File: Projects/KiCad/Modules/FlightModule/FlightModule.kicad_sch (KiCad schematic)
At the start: 59 parts, among them J1 Conn_01x08, J2 Conn_01x02_Pin, J3 Conn_01x02_Pin, J4 Conn_01x02_Pin, J5 Conn_01x02_Pin, J6 Conn_01x02_Pin, Q1 DTC143E, SW1 SW_DIP_x02, U1 MCP2562-E-P, U2 NUCLEO-F303K8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

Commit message: チップ積層セラミックコンデンサをSMD1608に変更
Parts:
- C1, C2, C4: footprint Capacitor_SMD:C_0805_2012Metric_Pad1.18x1.45mm_HandSolder -> Capacitor_SMD:C_0603_1608Metric_Pad1.08x0.95mm_HandSolder
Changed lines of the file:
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@@
       (effects (font (size 1.27 1.27)) (justify left))
     )
-    (property "Footprint" "Capacitor_SMD:C_0805_2012Metric_Pad1.18x1.45mm_HandSolder" (at 88.5952 35.56 0)
+    (property "Footprint" "Capacitor_SMD:C_0603_1608Metric_Pad1.08x0.95mm_HandSolder" (at 88.5952 35.56 0)
       (effects (font (size 1.27 1.27)) hide)
     )
@@
       (effects (font (size 1.27 1.27)) (justify left))
     )
-    (property "Footprint" "Capacitor_SMD:C_0805_2012Metric_Pad1.18x1.45mm_HandSolder" (at 79.7052 35.56 0)
+    (property "Footprint" "Capacitor_SMD:C_0603_1608Metric_Pad1.08x0.95mm_HandSolder" (at 79.7052 35.56 0)
       (effects (font (size 1.27 1.27)) hide)
     )
@@
       (effects (font (size 1.27 1.27)) (justify left))
     )
-    (property "Footprint" "Capacitor_SMD:C_0805_2012Metric_Pad1.18x1.45mm_HandSolder" (at 121.6152 109.22 0)
-      (effects (font (size 1.27 1.27)) hide)
-    )
+    (property "Footprint" "Capacitor_SMD:C_0603_1608Metric_Pad1.08x0.95mm_HandSolder" (at 121.6152 109.22 0)
+      (effects (font (size 1.27 1.27)) hide)
+    )

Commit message: 抵抗の在庫に合わせてサイズを変更
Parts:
- R23, R24, R5, R6: footprint Resistor_SMD:R_0603_1608Metric_Pad0.98x0.95mm_HandSolder -> Resistor_SMD:R_0805_2012Metric_Pad1.20x1.40mm_HandSolder
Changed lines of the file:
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@@
       (effects (font (size 1.27 1.27)) (justify left))
     )
-    (property "Footprint" "Resistor_SMD:R_0603_1608Metric_Pad0.98x0.95mm_HandSolder" (at 106.172 92.71 90)
+    (property "Footprint" "Resistor_SMD:R_0805_2012Metric_Pad1.20x1.40mm_HandSolder" (at 106.172 92.71 90)
       (effects (font (size 1.27 1.27)) hide)
     )
@@
       (effects (font (size 1.27 1.27)) (justify left))
     )
-    (property "Footprint" "Resistor_SMD:R_0603_1608Metric_Pad0.98x0.95mm_HandSolder" (at 182.372 49.53 90)
+    (property "Footprint" "Resistor_SMD:R_0805_2012Metric_Pad1.20x1.40mm_HandSolder" (at 182.372 49.53 90)
       (effects (font (size 1.27 1.27)) hide)
     )
@@
       (effects (font (size 1.27 1.27)))
     )
-    (property "Footprint" "Resistor_SMD:R_0603_1608Metric_Pad0.98x0.95mm_HandSolder" (at 114.3 97.282 90)
+    (property "Footprint" "Resistor_SMD:R_0805_2012Metric_Pad1.20x1.40mm_HandSolder" (at 114.3 97.282 90)
       (effects (font (size 1.27 1.27)) hide)
     )
@@
       (effects (font (size 1.27 1.27)) (justify left))
     )
-    (property "Footprint" "Resistor_SMD:R_0603_1608Metric_Pad0.98x0.95mm_HandSolder" (at 172.212 49.53 90)
-      (effects (font (size 1.27 1.27)) hide)
-    )
+    (property "Footprint" "Resistor_SMD:R_0805_2012Metric_Pad1.20x1.40mm_HandSolder" (at 172.212 49.53 90)
+      (effects (font (size 1.27 1.27)) hide)
+    )

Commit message: コネクタのピン配置を変更
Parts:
- J1: footprint Connector_Hirose:Hirose_DF11-8DP-2DSA_2x04_P2.00mm_Vertical -> Hirose_Connector:Hirose_DF11B-8DP-2DS
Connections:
- net CAN_L: now also J1.5 (Pin_5), J1.6 (Pin_6); no longer J1.3 (Pin_3), J1.4 (Pin_4)
- net GND: now also J1.3 (Pin_3), J1.4 (Pin_4); no longer J1.5 (Pin_5), J1.6 (Pin_6)
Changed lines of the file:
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@@
-    (effects (font (size 1.27 1.27)) (justify right bottom))
-  )
-  (label "CAN_L" (at 36.83 36.83 180) (fields_autoplaced)
-    (effects (font (size 1.27 1.27)) (justify right bottom))
-  )
-  (label "GND" (at 36.83 31.75 180) (fields_autoplaced)
     (effects (font (size 1.27 1.27)) (justify right bottom))
   )
@@
     (effects (font (size 1.27 1.27)) (justify right bottom))
   )
+  (label "GND" (at 36.83 36.83 180) (fields_autoplaced)
+    (effects (font (size 1.27 1.27)) (justify right bottom))
+  )
   (label "GND" (at 41.91 57.15 0) (fields_autoplaced)
     (effects (font (size 1.27 1.27)) (justify left bottom))
   )
+  (label "CAN_H" (at 36.83 26.67 180) (fields_autoplaced)
+    (effects (font (size 1.27 1.27)) (justify right bottom))
+  )
   (label "+12V" (at 41.91 54.61 0) (fields_autoplaced)
     (effects (font (size 1.27 1.27)) (justify left bottom))
   )
-  (label "CAN_H" (at 36.83 26.67 180) (fields_autoplaced)
+  (label "CAN_L" (at 36.83 31.75 180) (fields_autoplaced)
     (effects (font (size 1.27 1.27)) (justify right bottom))
   )
@@
       (effects (font (size 1.27 1.27)))
     )
-    (property "Footprint" "Connector_Hirose:Hirose_DF11-8DP-2DSA_2x04_P2.00mm_Vertical" (at 20.32 35.56 0)
-      (effects (font (size 1.27 1.27)) hide)
-    )
+    (property "Footprint" "Hirose_Connector:Hirose_DF11B-8DP-2DS" (at 20.32 35.56 0)
+      (effects (font (size 1.27 1.27)) hide)
+    )

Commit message: バッファコンデンサを表面実装に変更
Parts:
- C3: value 100μF -> 47μF; footprint Capacitor_SMD:CP_Elec_6.3x7.7 -> Capacitor_SMD:CP_Elec_6.3x5.9
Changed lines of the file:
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@@
       (effects (font (size 1.27 1.27)) (justify left))
     )
-    (property "Value" "100μF" (at 186.69 124.206 0)
+    (property "Value" "47μF" (at 186.69 124.206 0)
       (effects (font (size 1.27 1.27)) (justify left))
     )
-    (property "Footprint" "Capacitor_SMD:CP_Elec_6.3x7.7" (at 183.8452 127 0)
+    (property "Footprint" "Capacitor_SMD:CP_Elec_6.3x5.9" (at 183.8452 127 0)
       (effects (font (size 1.27 1.27)) hide)
     )

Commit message: チェックよし（多分）
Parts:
- removed Q1: DTC143E, Package_TO_SOT_THT:TO-92_Inline, symbol Transistor_BJT:DTC143E
- added Q1: Q_NPN_BEC, Package_TO_SOT_SMD:SC-59_Handsoldering, symbol Device:Q_NPN_BEC
- added R26, R27: 4.7kΩ, Resistor_SMD:R_0603_1608Metric_Pad0.98x0.95mm_HandSolder, symbol Device:R
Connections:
- net CONTROL_CAMERA: now also R26.1
- net at J6.1 (Pin_1): now also Q1.2 (E), R27.1
- net at J6.2 (Pin_2): now also Q1.3 (C)
- new net: Q1.1 (B), R26.2, R27.2
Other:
- moved on the sheet: D10, J6, R13

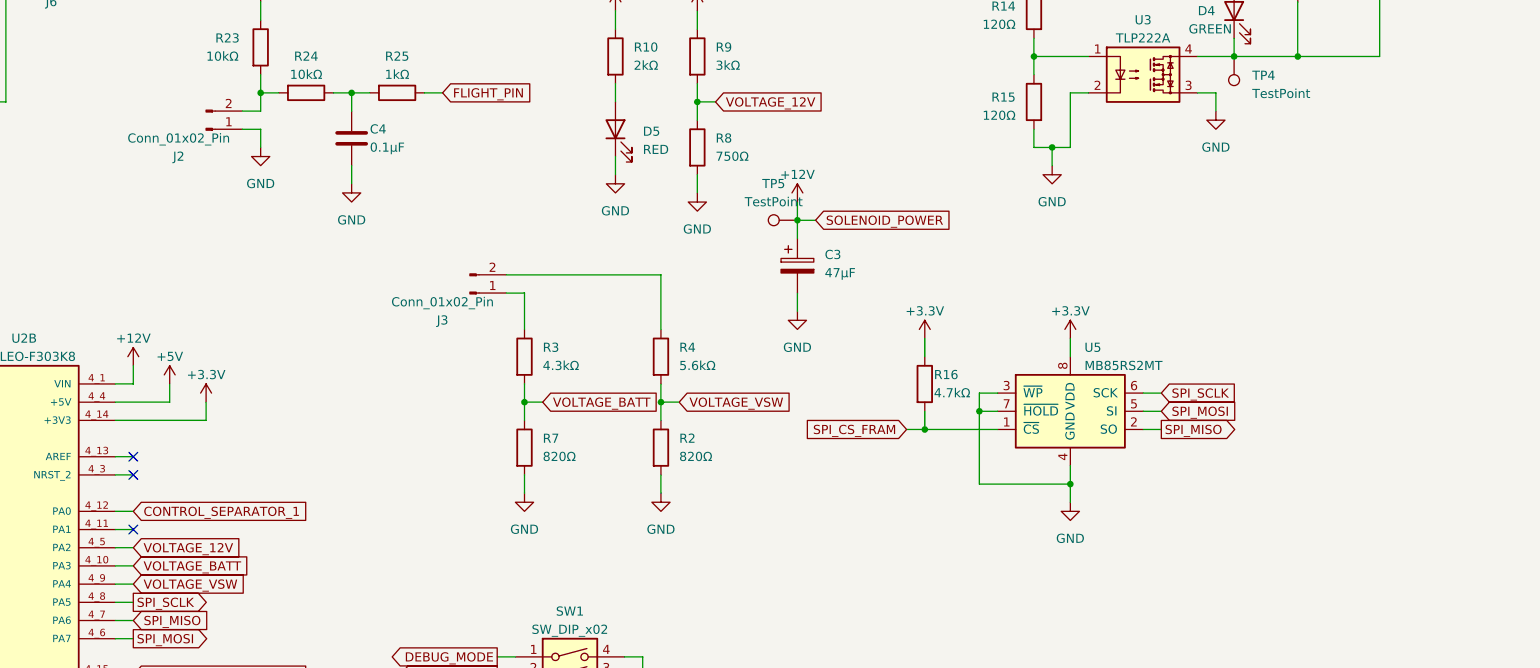
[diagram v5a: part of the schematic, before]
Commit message: フライトモジュールにブザーを追加
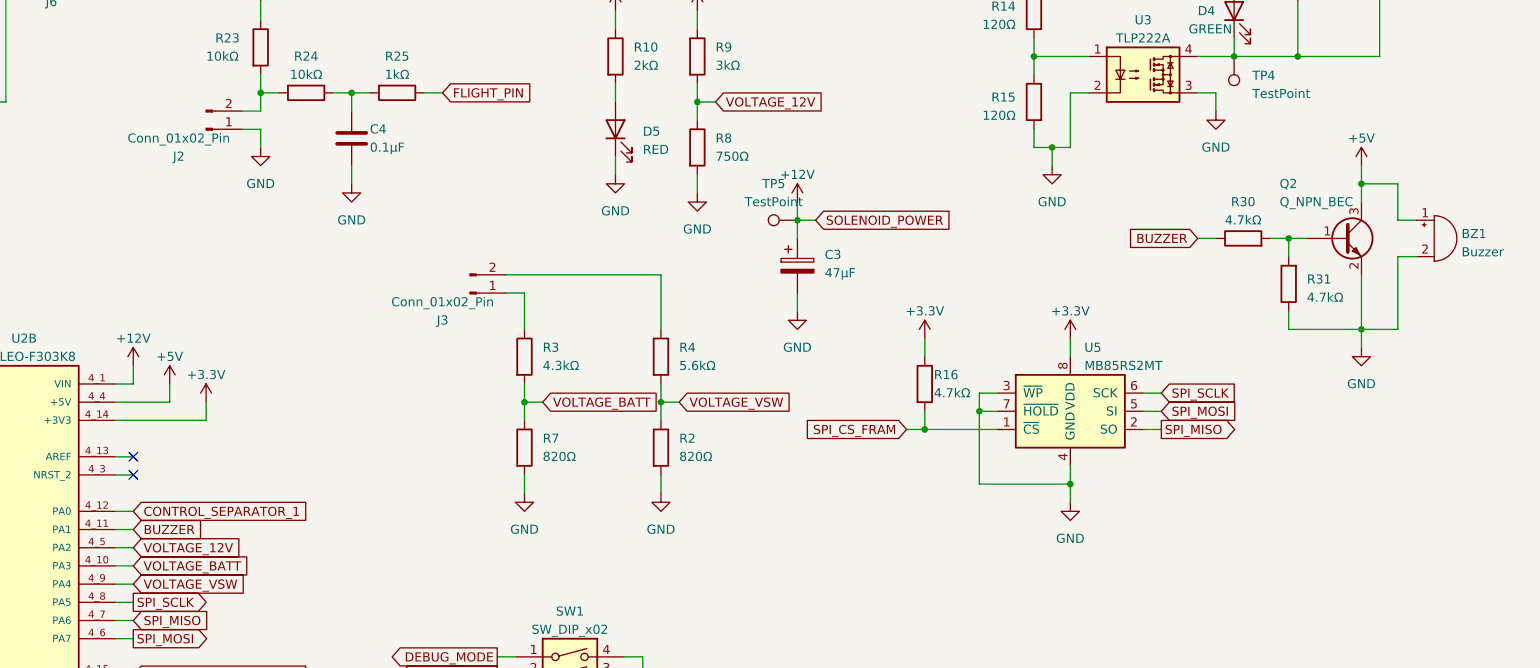
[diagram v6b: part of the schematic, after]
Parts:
- added BZ1: Buzzer, Buzzer_Beeper:Buzzer_12x9.5RM7.6, symbol Device:Buzzer
- added Q2: Q_NPN_BEC, Package_TO_SOT_SMD:SC-59_Handsoldering, symbol Device:Q_NPN_BEC
- added R30, R31: 4.7kΩ, Resistor_SMD:R_0603_1608Metric_Pad0.98x0.95mm_HandSolder, symbol Device:R
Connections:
- net +5V: now also BZ1.1 (-), Q2.3 (C)
- net GND: now also BZ1.2 (+), Q2.2 (E), R31.1
- net BUZZER: now reaches U2.4_11 (PA1)
- net BUZZER: now also R30.1
- new net: Q2.1 (B), R30.2, R31.2
- no-connect marks 4 -> 3

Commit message: フライトモジュールのGNDにテストポイントを追加
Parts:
- added TP6: TestPoint, Connector_Pin:Pin_D1.0mm_L10.0mm, symbol Connector:TestPoint
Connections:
- net GND: now also TP6.1
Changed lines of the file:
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@@
   (junction (at 200.66 146.05) (diameter 0) (color 0 0 0 0)
+  )
+  (junction (at 53.34 57.15) (diameter 0) (color 0 0 0 0)
   )
   (junction (at 261.62 132.08) (diameter 0) (color 0 0 0 0)
@@
         )
       )
+    )
+  )
+  (symbol (lib_id "Connector:TestPoint") (at 53.34 57.15 270) (unit 1)
+    (in_bom yes) (on_board yes) (dnp no) (fields_autoplaced)
+    (property "Reference" "TP6" (at 58.42 56.515 90)
+      (effects (font (size 1.27 1.27)) (justify left))
+    )
+    (property "Value" "TestPoint" (at 58.42 59.055 90)
+      (effects (font (size 1.27 1.27)) (justify left))
+    )
+    (property "Footprint" "Connector_Pin:Pin_D1.0mm_L10.0mm" (at 53.34 62.23 0)
+      (effects (font (size 1.27 1.27)) hide)
+    )
+    (property "Datasheet" "~" (at 53.34 62.23 0)
+      (effects (font (size 1.27 1.27)) hide)
+    )
+    (pin "1")
+    (instances
+      (project "FlightModule"
+        (path "/ea1ed597-7cd3-4340-902e-bdce8f2d7a62"
+          (reference "TP6") (unit 1)
+        )
+      )

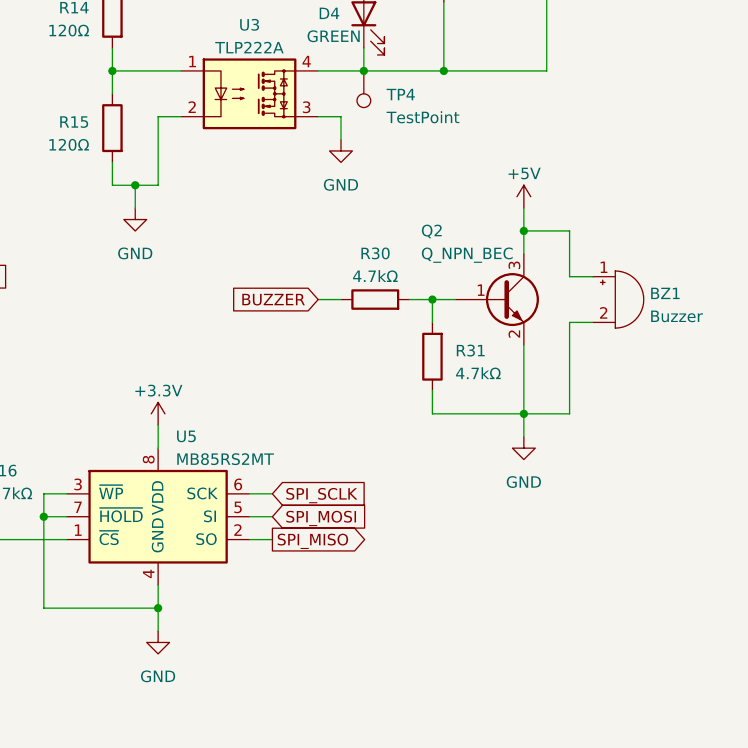
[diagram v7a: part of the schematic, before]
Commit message: ブザーの回路を修正
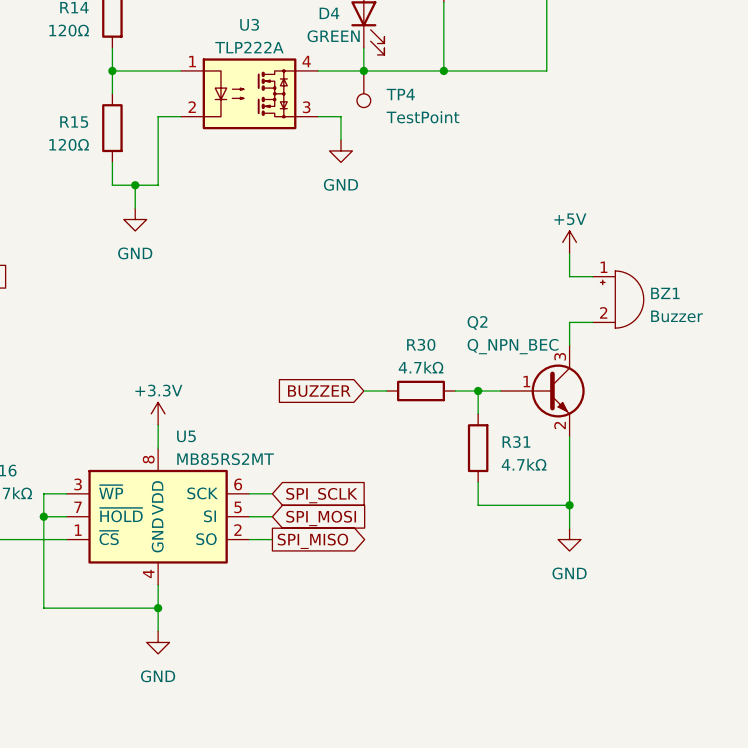
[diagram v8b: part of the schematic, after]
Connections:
- net +5V: no longer Q2.3 (C)
- net GND: no longer BZ1.2 (+)
- new net: BZ1.2 (+), Q2.3 (C)
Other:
- moved on the sheet: Q2, R30, R31
